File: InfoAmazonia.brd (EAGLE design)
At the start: 57 parts, among them IC1 LM2662, IC2 ADAFRUIT_FONA, IC3 MIC29302AWD, IC4 4050D, IC5 TL032C, IC6 CA3140AM Z, IC7 TL081BCDG4, IC8 SHT20, J1 BNCPTH, J2 BNCPTH, J3 BNCPTH, U1 ARDUINO-MEGAPRO, U2 MPL3115A2, U3 USD-SOCKETNEW, U4 ALS_PT19

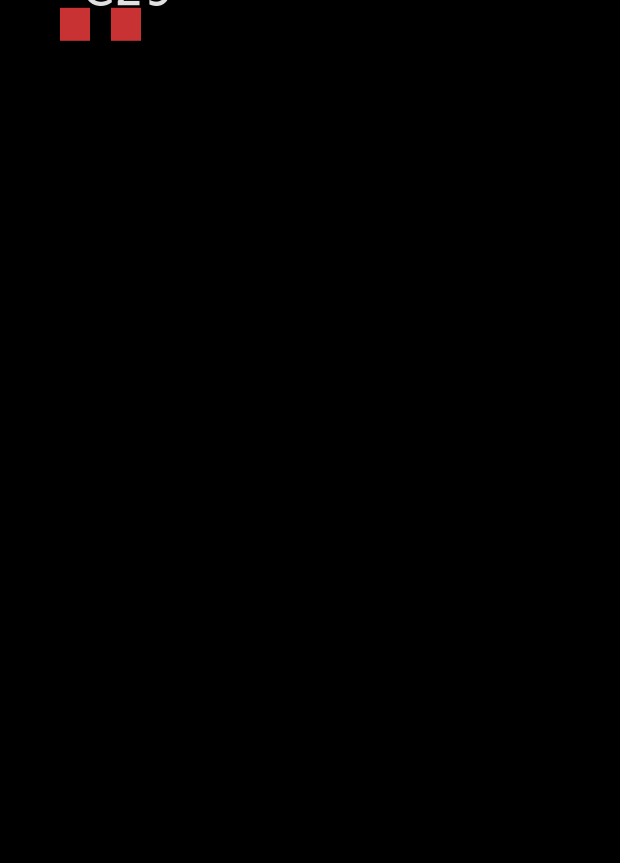
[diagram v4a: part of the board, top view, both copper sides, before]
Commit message: - Adicionado sensor de EC
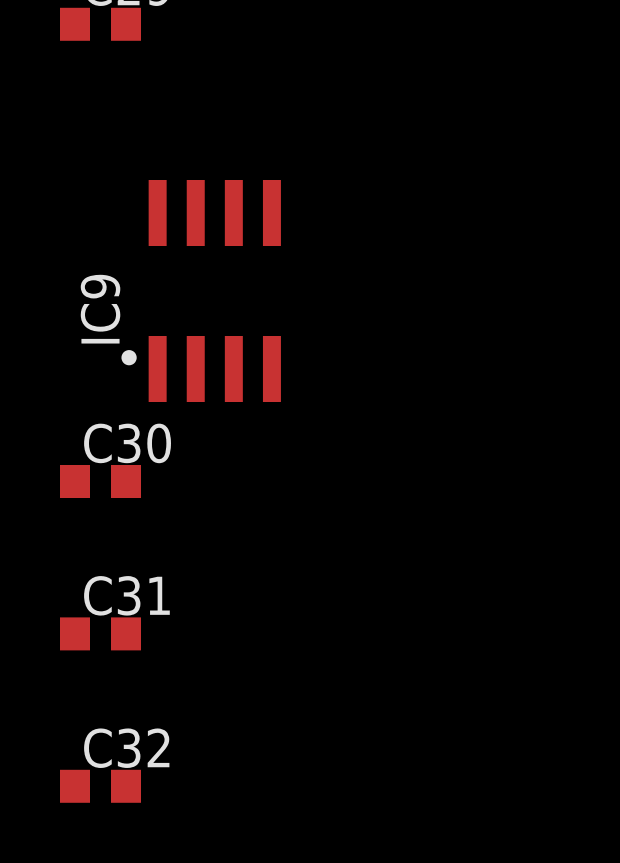
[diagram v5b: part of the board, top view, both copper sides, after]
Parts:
- added C30, C31: 100nF, InfoAmazonia:C0603
- added C32: 1uF, InfoAmazonia:C0603
- added IC9: NE555, InfoAmazonia:SO8
- R13: value 2k2 -> 10k
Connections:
- new net N$10: C30.1, IC9.5
- new net N$11: C32.1, IC9.2, IC9.6, J3.GND
- new net N$12: IC9.3, J3.S
- new net SCL: IC8.6, U2.8
- new net SDA: IC8.1, U2.7
- net +5V: now also C31.1, IC9.4, IC9.8
- net +VBAT: now also IC2.1
- net GND: now also C30.2, C31.2, C32.2, IC2.2, IC2.K1, IC2.K2, IC9.1
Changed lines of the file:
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@@
 <attribute name="PROD_ID" value="IC-11836" x="60.96" y="7.62" size="1.778" layer="27" rot="R270" display="off"/>
 </element>
-<element name="R13" library="InfoAmazonia" package="R0603" value="2k2" x="59.055" y="7.62" rot="R270"/>
+<element name="R13" library="InfoAmazonia" package="R0603" value="10k" x="59.055" y="7.62" rot="R270"/>
 <element name="J3" library="InfoAmazonia" package="BNC" value="BNCPTH" x="73.66" y="38.1"/>
 <element name="C29" library="InfoAmazonia" package="C0603" value="10uF" x="-2.54" y="-3.81"/>
+<element name="IC9" library="InfoAmazonia" package="SO8" value="NE555" x="1.27" y="-12.7"/>
+<element name="C30" library="InfoAmazonia" package="C0603" value="100nF" x="-2.54" y="-19.05"/>
+<element name="C31" library="InfoAmazonia" package="C0603" value="100nF" x="-2.54" y="-24.13"/>
+<element name="C32" library="InfoAmazonia" package="C0603" value="1uF" x="-2.54" y="-29.21"/>
 </elements>
 <signals>
@@
 <contactref element="C26" pad="2"/>
 <contactref element="C29" pad="2"/>
+<contactref element="IC9" pad="1"/>
+<contactref element="C30" pad="2"/>
+<contactref element="C32" pad="2"/>
+<contactref element="C31" pad="2"/>
+<contactref element="IC2" pad="K1"/>
+<contactref element="IC2" pad="2"/>
+<contactref element="IC2" pad="K2"/>
 <wire x1="82.55" y1="7.62" x2="85.09" y2="7.62" width="0" layer="19" extent="1-1"/>
 <wire x1="77.47" y1="8.47" x2="82.55" y2="7.62" width="0" layer="19" extent="1-1"/>
@@
 <wire x1="31.75" y1="2.54" x2="39.31" y2="6.985" width="0" layer="19" extent="1-1"/>
 <wire x1="29.21" y1="2.54" x2="31.75" y2="2.54" width="0" layer="19" extent="1-1"/>
-<wire x1="25.21" y1="9.525" x2="29.21" y2="2.54" width="0" layer="19" extent="1-1"/>
+<wire x1="29.21" y1="6.985" x2="29.21" y2="2.54" width="0" layer="19" extent="1-1"/>
+<wire x1="25.21" y1="9.525" x2="29.21" y2="6.985" width="0" layer="19" extent="1-1"/>
 <wire x1="25.21" y1="15.875" x2="25.21" y2="9.525" width="0" layer="19" extent="1-1"/>
 <wire x1="25.21" y1="22.225" x2="25.21" y2="15.875" width="0" layer="19" extent="1-1"/>
@@
 <wire x1="16.11" y1="40.495" x2="16.11" y2="34.795" width="0" layer="19" extent="1-1"/>
 <wire x1="23.71" y1="41.275" x2="16.11" y2="40.495" width="0" layer="19" extent="1-1"/>
+<wire x1="27.305" y1="47.625" x2="23.71" y2="41.275" width="0" layer="19" extent="1-1"/>
 <wire x1="14.605" y1="20.6375" x2="19.7866" y2="29.21" width="0" layer="19" extent="1-1"/>
 <wire x1="14.605" y1="13.97" x2="14.605" y2="20.6375" width="0" layer="19" extent="1-1"/>
 <wire x1="11.85" y1="10.16" x2="14.605" y2="13.97" width="0" layer="19" extent="1-1"/>
 <wire x1="4" y1="12.7" x2="11.85" y2="10.16" width="0" layer="19" extent="1-1"/>
+<wire x1="2.54" y1="6.985" x2="4" y2="12.7" width="0" layer="19" extent="1-1"/>
 <wire x1="4" y1="19.05" x2="4" y2="12.7" width="0" layer="19" extent="1-1"/>
 <wire x1="1.96" y1="28.945" x2="4" y2="19.05" width="0" layer="19" extent="1-1"/>
@@
 <wire x1="5.61" y1="39.105" x2="16.11" y2="40.495" width="0" layer="19" extent="1-1"/>
 <wire x1="2.96" y1="42.095" x2="5.61" y2="39.105" width="0" layer="19" extent="1-1"/>
-<wire x1="-1.69" y1="-3.81" x2="4" y2="12.7" width="0" layer="19" extent="1-1"/>
+<wire x1="-1.69" y1="-3.81" x2="2.54" y2="6.985" width="0" layer="19" extent="1-1"/>
+<wire x1="-0.635" y1="-15.3" x2="-1.69" y2="-3.81" width="0" layer="19" extent="1-1"/>
+<wire x1="-1.69" y1="-19.05" x2="-0.635" y2="-15.3" width="0" layer="19" extent="1-1"/>
+<wire x1="-1.69" y1="-24.13" x2="-1.69" y2="-19.05" width="0" layer="19" extent="1-1"/>
+<wire x1="-1.69" y1="-29.21" x2="-1.69" y2="-24.13" width="0" layer="19" extent="1-1"/>
 </signal>
 <signal name="+5V">
@@
 <contactref element="C22" pad="1"/>
 <contactref element="C23" pad="1"/>
+<contactref element="IC9" pad="4"/>
+<contactref element="IC9" pad="8"/>
+<contactref element="C31" pad="1"/>
 <wire x1="82.55" y1="50.8" x2="85.09" y2="50.8" width="0" layer="19" extent="1-1"/>
 <wire x1="53.76" y1="26.67" x2="82.55" y2="50.8" width="0" layer="19" extent="1-1"/>
@@
 <wire x1="38.1" y1="22.01" x2="40.64" y2="22.01" width="0" layer="19" extent="1-1"/>
 <wire x1="36.77" y1="26.035" x2="38.1" y2="22.01" width="0" layer="19" extent="1-1"/>
-<wire x1="42.76" y1="11.43" x2="40.64" y2="22.01" width="0" layer="19" extent="1-1"/>
-<wire x1="44.51" y1="9.525" x2="42.76" y2="11.43" width="0" layer="19" extent="1-1"/>
+<wire x1="44.51" y1="9.525" x2="52.705" y2="16.295" width="0" layer="19" extent="1-1"/>
+<wire x1="42.76" y1="11.43" x2="44.51" y2="9.525" width="0" layer="19" extent="1-1"/>
 <wire x1="26.67" y1="2.54" x2="42.76" y2="11.43" width="0" layer="19" extent="1-1"/>
 <wire x1="13.335" y1="13.97" x2="26.67" y2="2.54" width="0" layer="19" extent="1-1"/>
 <wire x1="8.7" y1="12.7" x2="13.335" y2="13.97" width="0" layer="19" extent="1-1"/>
 <wire x1="8.7" y1="19.05" x2="8.7" y2="12.7" width="0" layer="19" extent="1-1"/>
+<wire x1="-0.635" y1="-10.1" x2="8.7" y2="12.7" width="0" layer="19" extent="1-1"/>
+<wire x1="3.175" y1="-15.3" x2="-0.635" y2="-10.1" width="0" layer="19" extent="1-1"/>
+<wire x1="-3.39" y1="-24.13" x2="3.175" y2="-15.3" width="0" layer="19" extent="1-1"/>
 </signal>
 <signal name="+3V3">
@@
 <contactref element="C6" pad="+"/>
 <contactref element="R2" pad="1"/>
+<contactref element="IC2" pad="1"/>
+<wire x1="20.51" y1="22.225" x2="29.845" y2="47.625" width="0" layer="19" extent="1-1"/>
 <wire x1="20.51" y1="15.875" x2="20.51" y2="22.225" width="0" layer="19" extent="1-1"/>
 <wire x1="15.875" y1="13.97" x2="20.51" y2="15.875" width="0" layer="19" extent="1-1"/>
@@
 <wire x1="59.055" y1="6.77" x2="60.96" y2="6.87" width="0" layer="19" extent="1-1"/>
 </signal>
+<signal name="N$10">
+<contactref element="IC9" pad="5"/>
+<contactref element="C30" pad="1"/>
+<wire x1="3.175" y1="-10.1" x2="-3.39" y2="-19.05" width="0" layer="19" extent="1-1"/>
+</signal>
+<signal name="N$11">
+<contactref element="IC9" pad="6"/>
+<contactref element="IC9" pad="2"/>
+<contactref element="C32" pad="1"/>
+<contactref element="J3" pad="GND"/>
+<wire x1="1.905" y1="-10.1" x2="71.12" y2="38.1" width="0" layer="19" extent="1-1"/>
+<wire x1="0.635" y1="-15.3" x2="1.905" y2="-10.1" width="0" layer="19" extent="1-1"/>
+<wire x1="-3.39" y1="-29.21" x2="0.635" y2="-15.3" width="0" layer="19" extent="1-1"/>
+</signal>
+<signal name="N$12">
+<contactref element="IC9" pad="3"/>
+<contactref element="J3" pad="S"/>
+<wire x1="1.905" y1="-15.3" x2="73.66" y2="38.1" width="0" layer="19" extent="1-1"/>
+</signal>
+<signal name="SDA">
+<contactref element="IC8" pad="1"/>
+<contactref element="U2" pad="7"/>
+<wire x1="67.935" y1="6.42" x2="75.295" y2="9.02" width="0" layer="19" extent="1-1"/>
+</signal>
+<signal name="SCL">
+<contactref element="IC8" pad="6"/>
+<contactref element="U2" pad="8"/>
+<wire x1="69.185" y1="6.42" x2="75.295" y2="6.12" width="0" layer="19" extent="1-1"/>
+</signal>
 </signals>

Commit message: - Terminado o esquematico
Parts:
- added JP1, JP10, JP11, JP12, JP13, JP2, JP3, JP4, JP5, JP6, JP7, JP8, JP9: (no value), InfoAmazonia:1X03
- added R14, R15, R16: 0, InfoAmazonia:R0603
- added R17: 4k7, InfoAmazonia:R0603
- IC2: value ADAFRUIT_FONA -> ADAFRUIT FONA
- U4: value ALS_PT19 -> ALS-PT19
- moved C32 125.0 mm to (71.1, 71.8)
- moved C31 119.4 mm to (74.9, 66.7), turned to 90 degrees
- moved C30 110.6 mm to (67.3, 66.7), turned to 90 degrees
- moved IC9 105.7 mm to (71.1, 66.7), turned to 180 degrees
- moved R10 56.5 mm to (48.3, 71.8), turned to 180 degrees
- moved R8 55.8 mm to (52.1, 68.6), turned to 270 degrees
- moved C21 54.6 mm to (14.6, 71.8), turned to 0 degrees
- moved R7 53.8 mm to (10.8, 71.8), turned to 0 degrees
- moved C26 51.8 mm to (44.5, 70.5), turned to 90 degrees
- moved R12 51.6 mm to (52.1, 64.8), turned to 270 degrees
- moved C17 50.5 mm to (17.8, 67.9), turned to 180 degrees
- moved IC7 50.4 mm to (48.3, 66.7), turned to 180 degrees
- moved R6 50.4 mm to (36.8, 73.0), turned to 180 degrees
- moved C29 50.2 mm to (8.89, 45.1), turned to 180 degrees
- moved C20 49.4 mm to (36.8, 70.5)
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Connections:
- removed net OPR_SENSOR: IC5.7, R11.2
- new net 1_SENSOR: JP10.1, R16.2, U1.A2
- new net 2_SENSOR: JP11.1, R15.2, U1.A3
- new net 3_SENSOR: JP12.1, R14.2, U1.A4
- new net EC_IN: C32.1, IC9.2, IC9.6, JP4.3
- new net EC_SENSOR: IC9.3, JP3.1, JP4.2
- new net EN_BAT: IC3.1, U1.13
- new net FREQ_SENSOR: R14.1, R15.1, R16.1, U1.49
- new net GSM_KEY: IC2.7, U1.10
- new net GSM_NS: IC2.11, U1.7
- new net GSM_PT: IC2.6, U1.11
- new net GSM_RI: IC2.8, U1.2
- new net GSM_RST: IC2.5, U1.12
- new net GSM_RX: IC2.10, U1.8
- new net GSM_TX: IC2.9, U1.9
- new net INT1: U1.18, U2.6
- new net INT2: U1.19, U2.5
- new net LUZ_SENSOR: R13.2, U1.A5, U4.E
- new net N$22: J3.GND, JP5.2
- new net ORP_IN: IC5.3, JP8.3
- new net ORP_SENSOR: IC5.7, JP7.1, R11.2
- new net PH_IN: JP2.3, R3.1
- new net TEMP_SENSOR: JP13.2, R17.2, U1.A6
- net +5V: now also IC2.12, JP1.3, JP10.3, JP11.3, JP12.3, JP13.1, JP3.3, JP7.3, R17.1
- net -5V: now also JP1.2, JP10.2, JP11.2, JP12.2, JP3.2, JP7.2
- net GND: now also JP13.3, JP2.1, JP2.2, JP4.1, JP5.1, JP6.1, JP8.1, JP8.2, JP9.1; no longer J1.GND, J2.GND
- net N$1: now also J1.S, JP9.3; no longer J2.S, R3.1
- net N$11: now also J2.S, JP6.3; no longer C32.1, IC9.2, IC9.6, J3.GND
- net N$12: now also J2.GND, JP6.2; no longer IC9.3, J3.S
- net N$13: now also J3.S, JP5.3; no longer IC5.3, J1.S
- net N$9: now also J1.GND, JP9.2; no longer R13.2, U4.E
- net PH_SENSOR: now also JP1.1
- net SCL: now also U1.SCL
- net SDA: now also U1.SDA
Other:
- board outline added: 91.4 x 74.9 mm

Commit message: [INFOA-26]
- Mudanças de conector JST PH
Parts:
- removed JP13: (no value), InfoAmazonia:1X03
- removed R17: 4k7, InfoAmazonia:R0603
- added JP14, JP15, JP16, JP17: (no value), InfoAmazonia:JST-4-PTH-VERT
- moved C30 9.25 mm to (76.2, 64.1)
- moved C32 9.25 mm to (80.0, 69.2)
- moved IC9 9.25 mm to (80.0, 64.1)
- moved JP3 9.25 mm to (92.7, 64.1)
- moved JP4 9.25 mm to (68.6, 64.1)
- moved C31 9.25 mm to (83.8, 64.1)
- moved C19 4.58 mm to (37.5, 66.7)
- moved C20 4.58 mm to (40.6, 67.9)
- moved R5 4.58 mm to (45.1, 66.7)
- moved R6 4.58 mm to (40.6, 70.5)
- moved C15 4.58 mm to (36.2, 62.2)
- moved C18 4.58 mm to (36.2, 58.4)
- moved C22 4.58 mm to (52.1, 59.1)
- moved C9 4.58 mm to (44.5, 59.7)
- moved IC6 4.58 mm to (40.0, 60.3)
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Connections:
- new net +12V: C4.+, C5.+, IC3.2, U1.VIN
- new net A14: JP14.1, U1.A14
- new net A15: JP14.2, U1.A15
- new net RX2: JP17.1, U1.17
- new net RX3: JP16.1, U1.15
- new net TX2: JP17.2, U1.16
- new net TX3: JP16.2, U1.14
- net +5V: now also JP14.3, JP15.3, JP16.3, JP17.3; no longer C4.+, C5.+, IC3.2, JP13.1, R17.1
- net FREQ_SENSOR: now also U1.47
- net GND: now also JP14.4, JP15.4, JP16.4, JP17.4; no longer JP13.3
- net SCL: now also JP15.1
- net SDA: now also JP15.2
- net TEMP_SENSOR: no longer JP13.2, R17.2
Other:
- board size 91.4 x 74.9 mm -> 95.2 x 72.4 mm

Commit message: [INFOA-26]
- Placa roteada pelo Anderson
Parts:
- moved C30 11.4 mm to (65.0, 62.1)
- moved IC9 11.4 mm to (68.8, 62.1)
- moved JP4 11.4 mm to (57.4, 62.1)
- moved C31 11.4 mm to (72.6, 62.1)
- moved JP3 11.4 mm to (81.5, 62.1)
- moved C32 11.3 mm to (68.8, 67.5)
- moved R16 8.08 mm to (76.0, 20.3)
- moved R8 5.24 mm to (51.1, 64.0), turned to 90 degrees
- moved C18 5.24 mm to (31.4, 56.4)
- moved C24 5.24 mm to (43.4, 62.1)
- moved IC6 5.24 mm to (35.2, 58.3)
- moved IC7 5.24 mm to (47.2, 62.1)
- moved JP1 5.24 mm to (53.6, 62.1)
- moved JP2 5.24 mm to (29.5, 62.1)
- moved C15 5.24 mm to (31.4, 60.2)
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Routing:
- net +5V: track 0.00 -> 234.5 mm, vias 0 -> 5
- net SCL: track 0.00 -> 161.4 mm, vias 0 -> 1
- net GND: track 0.00 -> 158.3 mm, vias 0 -> 10
- net SDA: track 0.00 -> 156.1 mm, vias 0 -> 1
- net +3V3: track 0.00 -> 148.7 mm, vias 0 -> 2
- net -5V: track 0.00 -> 144.5 mm, vias 0 -> 4
- net MISO: track 0.00 -> 101.8 mm, vias 0 -> 2
- net CS_SD: track 0.00 -> 90.1 mm, vias 0 -> 2
- net MOSI: track 0.00 -> 85.2 mm
- net SCK: track 0.00 -> 81.7 mm, vias 0 -> 2
- net +12V: track 0.00 -> 65.8 mm
- net GSM_RI: track 0.00 -> 64.0 mm, vias 0 -> 2
- net INT1: track 0.00 -> 53.0 mm, vias 0 -> 3
- net INT2: track 0.00 -> 51.9 mm, vias 0 -> 3
- net GSM_NS: track 0.00 -> 50.6 mm
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- added copper zone on layer 1, net GND
- added copper zone on layer 16, net GND
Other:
- board size 95.2 x 72.4 mm -> 95.2 x 70.4 mm
